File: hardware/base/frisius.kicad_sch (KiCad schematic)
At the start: 0 parts

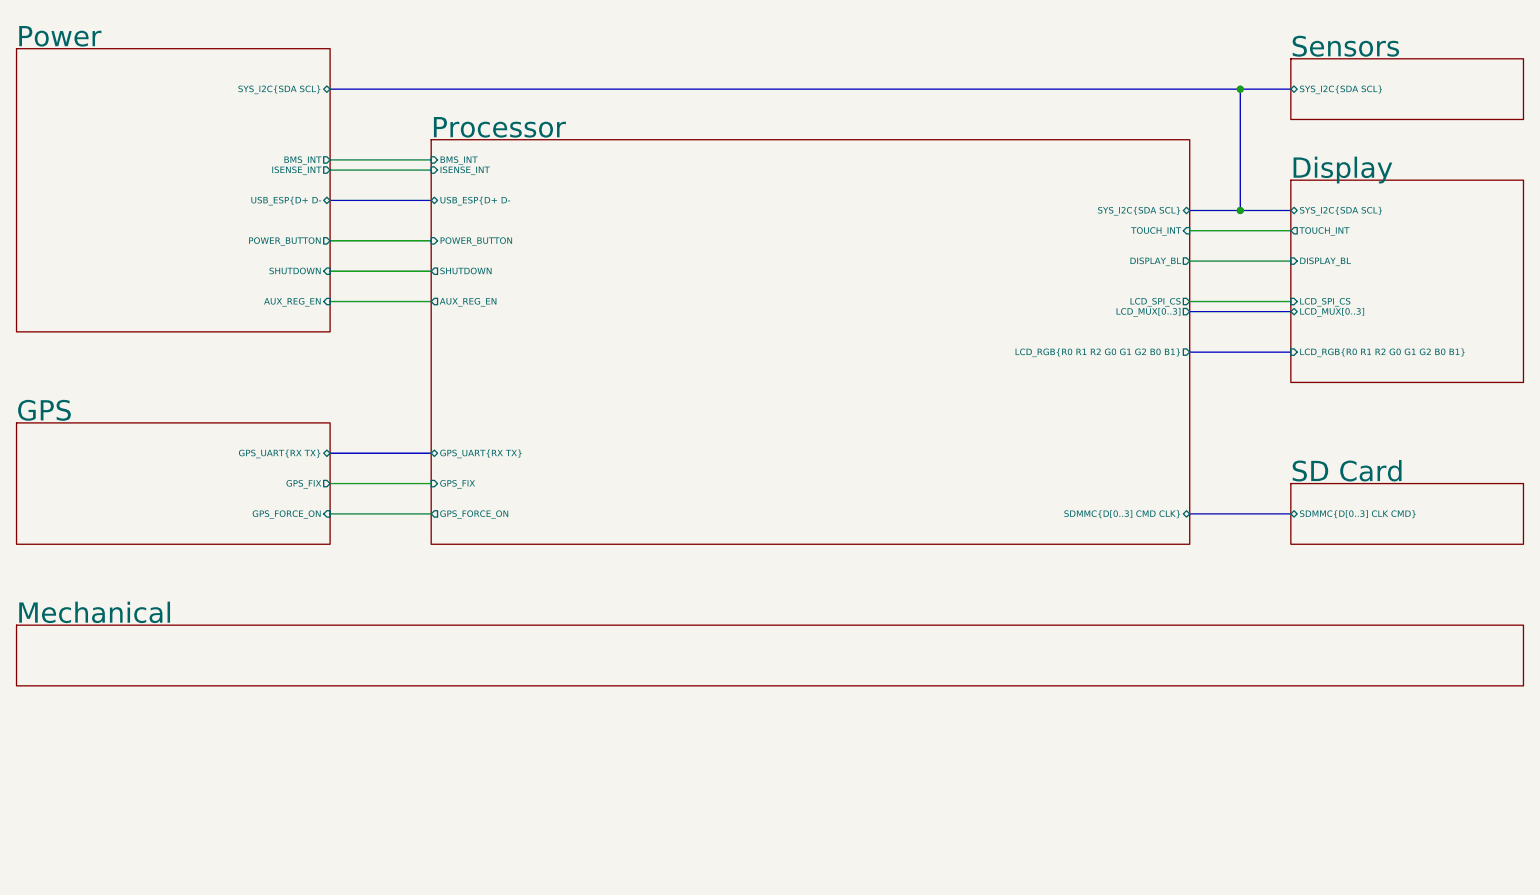
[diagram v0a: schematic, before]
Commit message: layout complete, drc checks and tweaks to silkscreen, attempting geo reannotate
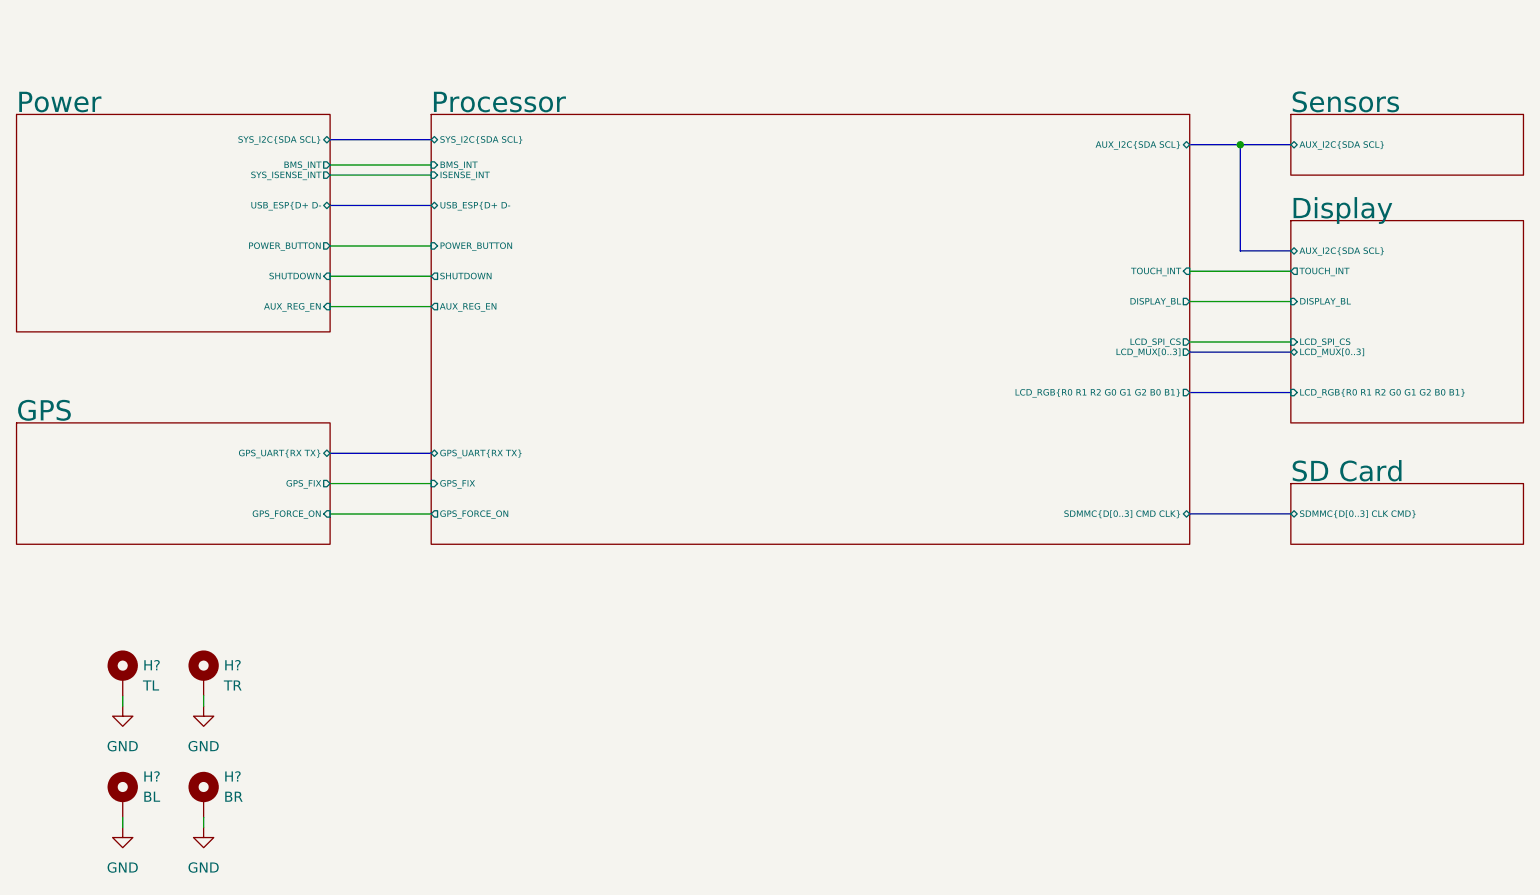
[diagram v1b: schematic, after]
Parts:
- added H?: BL, Mounting_Wuerth:Mounting_Wuerth_WA-SMSI-M1.6_H2mm_9774020633, symbol Mechanical:MountingHole_Pad
- added H?: BR, Mounting_Wuerth:Mounting_Wuerth_WA-SMSI-M1.6_H2mm_9774020633, symbol Mechanical:MountingHole_Pad
- added H?: TR, Mounting_Wuerth:Mounting_Wuerth_WA-SMSI-M1.6_H2mm_9774020633, symbol Mechanical:MountingHole_Pad
- added H?: TL, Mounting_Wuerth:Mounting_Wuerth_WA-SMSI-M1.6_H2mm_9774020633, symbol Mechanical:MountingHole_Pad
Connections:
- new net GND: H?.1, H?.1, H?.1, H?.1
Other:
- removed sheet Mechanical
- sheet Display ports: added AUX_I2C{SDA SCL}; removed SYS_I2C{SDA SCL}
- sheet Power ports: added SYS_ISENSE_INT; removed ISENSE_INT
- sheet Processor ports: added AUX_I2C{SDA SCL}; removed none
- sheet Sensors ports: added AUX_I2C{SDA SCL}; removed SYS_I2C{SDA SCL}

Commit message: Tidied up, added more stitches
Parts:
- gave numbers to parts that had none: 4
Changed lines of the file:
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@@
   (symbol (lib_id "power:GND") (at 69.215 134.62 0) (unit 1)
     (in_bom yes) (on_board yes) (fields_autoplaced)
-    (property "Reference" "#PWR?" (id 0) (at 69.215 140.97 0)
+    (property "Reference" "#PWR0151" (id 0) (at 69.215 140.97 0)
       (effects (font (size 1.27 1.27)) hide)
     )
@@
   (symbol (lib_id "power:GND") (at 59.055 134.62 0) (unit 1)
     (in_bom yes) (on_board yes) (fields_autoplaced)
-    (property "Reference" "#PWR?" (id 0) (at 59.055 140.97 0)
+    (property "Reference" "#PWR0152" (id 0) (at 59.055 140.97 0)
       (effects (font (size 1.27 1.27)) hide)
     )
@@
   (symbol (lib_id "power:GND") (at 59.055 149.86 0) (unit 1)
     (in_bom yes) (on_board yes) (fields_autoplaced)
-    (property "Reference" "#PWR?" (id 0) (at 59.055 156.21 0)
+    (property "Reference" "#PWR0149" (id 0) (at 59.055 156.21 0)
       (effects (font (size 1.27 1.27)) hide)
     )
@@
   (symbol (lib_id "Mechanical:MountingHole_Pad") (at 59.055 146.05 0) (unit 1)
     (in_bom yes) (on_board yes) (fields_autoplaced)
-    (property "Reference" "H?" (id 0) (at 61.595 143.5099 0)
+    (property "Reference" "H2" (id 0) (at 61.595 143.5099 0)
       (effects (font (size 1.27 1.27)) (justify left))
     )
@@
   (symbol (lib_id "Mechanical:MountingHole_Pad") (at 69.215 146.05 0) (unit 1)
     (in_bom yes) (on_board yes) (fields_autoplaced)
-    (property "Reference" "H?" (id 0) (at 71.755 143.5099 0)
+    (property "Reference" "H4" (id 0) (at 71.755 143.5099 0)
       (effects (font (size 1.27 1.27)) (justify left))
     )
@@
   (symbol (lib_id "power:GND") (at 69.215 149.86 0) (unit 1)
     (in_bom yes) (on_board yes) (fields_autoplaced)
-    (property "Reference" "#PWR?" (id 0) (at 69.215 156.21 0)
+    (property "Reference" "#PWR0150" (id 0) (at 69.215 156.21 0)
       (effects (font (size 1.27 1.27)) hide)
     )
@@
   (symbol (lib_id "Mechanical:MountingHole_Pad") (at 69.215 130.81 0) (unit 1)
     (in_bom yes) (on_board yes) (fields_autoplaced)
-    (property "Reference" "H?" (id 0) (at 71.755 129.5399 0)
+    (property "Reference" "H3" (id 0) (at 71.755 129.5399 0)
       (effects (font (size 1.27 1.27)) (justify left))
     )
@@
   (symbol (lib_id "Mechanical:MountingHole_Pad") (at 59.055 130.81 0) (unit 1)
     (in_bom yes) (on_board yes) (fields_autoplaced)
-    (property "Reference" "H?" (id 0) (at 61.595 129.5399 0)
+    (property "Reference" "H1" (id 0) (at 61.595 129.5399 0)
       (effects (font (size 1.27 1.27)) (justify left))
     )
@@
       (reference "#PWR0148") (unit 1) (value "GND") (footprint "")
     )
+    (path "/28ccd33f-7c09-4427-a810-2072c0f109f4"
+      (reference "#PWR0149") (unit 1) (value "GND") (footprint "")
+    )
+    (path "/3113954d-b76d-4d82-9a04-65d3ce9cd25a"
+      (reference "#PWR0150") (unit 1) (value "GND") (footprint "")
+    )
+    (path "/0b6eeb64-188f-44c7-ac5a-1741b24d7b7f"
+      (reference "#PWR0151") (unit 1) (value "GND") (footprint "")
+    )
+    (path "/0c23defb-105e-464b-8169-1a8c0df61355"
+      (reference "#PWR0152") (unit 1) (value "GND") (footprint "")
+    )
     (path "/d6a81b3b-912c-47c7-b234-5345a0da5522/192511b0-1269-4b3b-a3cb-9f5e6d5f8e19"
       (reference "#PWR0153") (unit 1) (value "VDD_CORE_3V3") (footprint "")
@@
       (reference "#PWR0163") (unit 1) (value "VDD_AUX_3V3") (footprint "")
     )
+    (path "/de840488-ca73-469b-adda-a3c2d8f9c87a/656a1aa6-83b0-4862-be2f-3f423f22c905"
+      (reference "#PWR0164") (unit 1) (value "GND") (footprint "")
+    )
     (path "/d6a81b3b-912c-47c7-b234-5345a0da5522/36c552b1-3458-4f15-8381-25605d32664b"
       (reference "#PWR0165") (unit 1) (value "VDD_NVDC") (footprint "")
@@
       (reference "#PWR0201") (unit 1) (value "GND") (footprint "")
     )
-    (path "/0b6eeb64-188f-44c7-ac5a-1741b24d7b7f"
-      (reference "#PWR?") (unit 1) (value "GND") (footprint "")
-    )
-    (path "/0c23defb-105e-464b-8169-1a8c0df61355"
-      (reference "#PWR?") (unit 1) (value "GND") (footprint "")
-    )
-    (path "/28ccd33f-7c09-4427-a810-2072c0f109f4"
-      (reference "#PWR?") (unit 1) (value "GND") (footprint "")
-    )
-    (path "/3113954d-b76d-4d82-9a04-65d3ce9cd25a"
-      (reference "#PWR?") (unit 1) (value "GND") (footprint "")
-    )
     (path "/1c2dbee6-2600-45d3-a892-1b4f3056883c/4a93e175-e777-4d61-a640-504f0de2dffd"
       (reference "#U0118") (unit 1) (value "VDD_AUX_3V3") (footprint "")
@@
       (reference "D7") (unit 1) (value "LED_Small_Filled") (footprint "LED_SMD:LED_0603_1608Metric")
     )
+    (path "/540523f8-1055-4635-9b1d-2957ff44902d"
+      (reference "H1") (unit 1) (value "TL") (footprint "Mounting_Wuerth:Mounting_Wuerth_WA-SMSI-M1.6_H2mm_9774020633")
+    )
     (path "/2ad0027e-87dd-40cf-b0af-f4f7822622e1"
-      (reference "H?") (unit 1) (value "BL") (footprint "Mounting_Wuerth:Mounting_Wuerth_WA-SMSI-M1.6_H2mm_9774020633")
+      (reference "H2") (unit 1) (value "BL") (footprint "Mounting_Wuerth:Mounting_Wuerth_WA-SMSI-M1.6_H2mm_9774020633")
+    )
+    (path "/425afff0-a816-49d5-b502-1f9df6e8fa18"
+      (reference "H3") (unit 1) (value "TR") (footprint "Mounting_Wuerth:Mounting_Wuerth_WA-SMSI-M1.6_H2mm_9774020633")
     )
     (path "/3049b83e-09c4-4570-bf9f-0f383c565431"
-      (reference "H?") (unit 1) (value "BR") (footprint "Mounting_Wuerth:Mounting_Wuerth_WA-SMSI-M1.6_H2mm_9774020633")
-    )
-    (path "/425afff0-a816-49d5-b502-1f9df6e8fa18"
-      (reference "H?") (unit 1) (value "TR") (footprint "Mounting_Wuerth:Mounting_Wuerth_WA-SMSI-M1.6_H2mm_9774020633")
-    )
-    (path "/540523f8-1055-4635-9b1d-2957ff44902d"
-      (reference "H?") (unit 1) (value "TL") (footprint "Mounting_Wuerth:Mounting_Wuerth_WA-SMSI-M1.6_H2mm_9774020633")
+      (reference "H4") (unit 1) (value "BR") (footprint "Mounting_Wuerth:Mounting_Wuerth_WA-SMSI-M1.6_H2mm_9774020633")
     )
     (path "/1c2dbee6-2600-45d3-a892-1b4f3056883c/34fc34eb-a9d0-4ff6-829a-aed671c67dca"
@@
       (reference "TP1") (unit 1) (value "GPS_FON") (footprint "TestPoint:TestPoint_Pad_D1.0mm")
     )
+    (path "/d09c9d73-a3ac-404b-b5ac-4477ad82de80/9da6ce66-df01-4c72-a992-89199af8ac7c"
+      (reference "TP2") (unit 1) (value "GPS_FON") (footprint "TestPoint:TestPoint_Pad_D1.0mm")
+    )
     (path "/d09c9d73-a3ac-404b-b5ac-4477ad82de80/27c44693-a2f9-4ad4-b5c5-59704384635d"
       (reference "TP14") (unit 1) (value "GPS_FON") (footprint "TestPoint:TestPoint_Pad_D1.0mm")
@@
     )
     (path "/de840488-ca73-469b-adda-a3c2d8f9c87a/ab16636a-57f9-4970-92b4-fe29e05d6e24"
-      (reference "U10") (unit 1) (value "TCA9801") (footprint "Package_SO:VSSOP-8_3.0x3.0mm_P0.65mm")
+      (reference "U10") (unit 1) (value "TCA9803") (footprint "Package_SO:VSSOP-8_3.0x3.0mm_P0.65mm")
     )
     (path "/d6a81b3b-912c-47c7-b234-5345a0da5522/d1b32182-a2e5-42d0-b8dc-e08ac1dd12e1"
